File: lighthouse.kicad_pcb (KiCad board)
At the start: 2 copper layers, 78 x 58 mm, 71 parts, among them J1 GT-USB-7010ASV, J10 From_E-stop, J11 From_E-stop, J2 Conn_01x05_Pin, J3 Conn_01x10_Pin, J4 From_E-stop, J5 694106301002, J6 From_E-stop, J7 From_E-stop, J8 From_E-stop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

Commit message: Renamifications
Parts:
- J1: footprint bedroom_lights:USB_C_Receptacle_G-Switch_GT-USB-7010ASV -> lighthouse:USB_C_Receptacle_G-Switch_GT-USB-7010ASV
- SW1, SW2: footprint bedroom_lights:TS-1088R-02026_SW_SMD_3x4mm -> lighthouse:TS-1088R-02026_SW_SMD_3x4mm
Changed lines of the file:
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@@
 		(property ki_fp_filters "MountingHole*Pad*")
 		(sheetname "/")
-		(sheetfile "bedroom_lights.kicad_sch")
+		(sheetfile "lighthouse.kicad_sch")
 		(attr exclude_from_pos_files exclude_from_bom)
 		(fp_circle
@@
 		)
 	)
-	(footprint "bedroom_lights:USB_C_Receptacle_G-Switch_GT-USB-7010ASV"
+	(footprint "lighthouse:USB_C_Receptacle_G-Switch_GT-USB-7010ASV"
 		(layer "F.Cu")
 		(at 188 68 90)
@@
 		(property ki_fp_filters "MountingHole*Pad*")
 		(sheetname "/")
-		(sheetfile "bedroom_lights.kicad_sch")
+		(sheetfile "lighthouse.kicad_sch")
 		(attr exclude_from_pos_files exclude_from_bom)
 		(fp_circle
@@
 		(property ki_fp_filters "MountingHole*Pad*")
 		(sheetname "/")
-		(sheetfile "bedroom_lights.kicad_sch")
+		(sheetfile "lighthouse.kicad_sch")
 		(attr exclude_from_pos_files exclude_from_bom)
 		(fp_circle
@@
 		(property ki_fp_filters "MountingHole*Pad*")
 		(sheetname "/")
-		(sheetfile "bedroom_lights.kicad_sch")
+		(sheetfile "lighthouse.kicad_sch")
 		(attr exclude_from_pos_files exclude_from_bom)
 		(fp_circle
@@
 		)
 	)
-	(footprint "bedroom_lights:TS-1088R-02026_SW_SMD_3x4mm"
+	(footprint "lighthouse:TS-1088R-02026_SW_SMD_3x4mm"
 		(layer "F.Cu")
 		(at 173 82.5 90)
@@
 		)
 	)
-	(footprint "bedroom_lights:TS-1088R-02026_SW_SMD_3x4mm"
+	(footprint "lighthouse:TS-1088R-02026_SW_SMD_3x4mm"
 		(layer "F.Cu")
 		(at 177 82.5 -90)

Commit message: Termianl block 3d view
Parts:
- J10, J11, J4, J6, J7, J8, J9: value From_E-stop -> TB0010-500-02GR; footprint TerminalBlock:TerminalBlock_MaiXu_MX126-5.0-02P_1x02_P5.00mm -> lighthouse:TerminalBlock_TB0010-500-02GR_1x02_P5.00mm
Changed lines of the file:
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@@
 		)
 	)
-	(footprint "TerminalBlock:TerminalBlock_MaiXu_MX126-5.0-02P_1x02_P5.00mm"
+	(footprint "lighthouse:TerminalBlock_TB0010-500-02GR_1x02_P5.00mm"
 		(layer "F.Cu")
 		(at 118 74.25 -90)
@@
 		(tags "THT terminal block MaiXu MX126-5.0-02P pitch 5mm size 10.5x7.8mm drill 1.3mm pad 2.8mm")
 		(property "Reference" "J8"
-			(at 4.59 24.52 90)
+			(at 2.25 -5.12 90)
 			(layer "F.SilkS")
 			(hide yes)
@@
 			)
 		)
-		(property "Value" "From_E-stop"
+		(property "Value" "TB0010-500-02GR"
 			(at 2.25 4.92 90)
 			(layer "F.Fab")
@@
 		)
 		(embedded_fonts no)
-		(model "${KICAD9_3DMODEL_DIR}/TerminalBlock.3dshapes/TerminalBlock_MaiXu_MX126-5.0-02P_1x02_P5.00mm.wrl"
+		(model "${KIPRJMOD}/3d/TB0010-500-02GR.stp"
 			(offset
-				(xyz 0 0 0)
+				(xyz 2.5 -0.5 6.25)
 			)
 			(scale
@@
 			)
 			(rotate
-				(xyz 0 0 0)
+				(xyz -90 -0 -0)
 			)
 		)
 	)
-	(footprint "TerminalBlock:TerminalBlock_MaiXu_MX126-5.0-02P_1x02_P5.00mm"
+	(footprint "lighthouse:TerminalBlock_TB0010-500-02GR_1x02_P5.00mm"
 		(layer "F.Cu")
 		(at 118 62.75 -90)
@@
 		(tags "THT terminal block MaiXu MX126-5.0-02P pitch 5mm size 10.5x7.8mm drill 1.3mm pad 2.8mm")
 		(property "Reference" "J9"
-			(at 2.31 -43.89 90)
+			(at 2.25 -5.12 90)
 			(layer "F.SilkS")
 			(hide yes)
@@
 			)
 		)
-		(property "Value" "From_E-stop"
+		(property "Value" "TB0010-500-02GR"
 			(at 2.25 4.92 90)
 			(layer "F.Fab")
@@
 		)
 		(embedded_fonts no)
-		(model "${KICAD9_3DMODEL_DIR}/TerminalBlock.3dshapes/TerminalBlock_MaiXu_MX126-5.0-02P_1x02_P5.00mm.wrl"
+		(model "${KIPRJMOD}/3d/TB0010-500-02GR.stp"
 			(offset
-				(xyz 0 0 0)
+				(xyz 2.5 -0.5 6.25)
 			)
 			(scale
@@
 			)
 			(rotate
-				(xyz 0 0 0)
+				(xyz -90 -0 -0)
 			)
 		)
@@
 		(embedded_fonts no)
 	)
-	(footprint "TerminalBlock:TerminalBlock_MaiXu_MX126-5.0-02P_1x02_P5.00mm"
+	(footprint "lighthouse:TerminalBlock_TB0010-500-02GR_1x02_P5.00mm"
 		(layer "F.Cu")
 		(at 186.9675 90.25 90)
@@
 		(tags "THT terminal block MaiXu MX126-5.0-02P pitch 5mm size 10.5x7.8mm drill 1.3mm pad 2.8mm")
 		(property "Reference" "J6"
-			(at 2.25 -5.12 90)
+			(at 2.25 -5.12 270)
 			(layer "F.SilkS")
 			(hide yes)
@@
 			)
 		)
-		(property "Value" "From_E-stop"
-			(at 2.25 4.92 90)
+		(property "Value" "TB0010-500-02GR"
+			(at 2.25 4.92 270)
 			(layer "F.Fab")
 			(effects
@@
 		)
 		(property "Datasheet" "~"
-			(at 0 0 90)
+			(at 0 0 270)
 			(layer "F.Fab")
 			(hide yes)
@@
 		)
 		(property "Description" "Generic screw terminal, single row, 01x02, script generated (kicad-library-utils/schlib/autogen/connector/)"
-			(at 0 0 90)
+			(at 0 0 270)
 			(layer "F.Fab")
 			(hide yes)
@@
 		)
 		(fp_text user "${REFERENCE}"
-			(at 2.25 2.65 90)
+			(at 2.25 2.65 270)
 			(layer "F.Fab")
 			(effects
@@
 		)
 		(embedded_fonts no)
-		(model "${KICAD9_3DMODEL_DIR}/TerminalBlock.3dshapes/TerminalBlock_MaiXu_MX126-5.0-02P_1x02_P5.00mm.wrl"
+		(model "${KIPRJMOD}/3d/TB0010-500-02GR.stp"
 			(offset
-				(xyz 0 0 0)
+				(xyz 2.5 -0.5 6.25)
 			)
 			(scale
@@
 			)
 			(rotate
-				(xyz 0 0 0)
+				(xyz -90 -0 -0)
 			)
 		)
@@
 		)
 	)
-	(footprint "TerminalBlock:TerminalBlock_MaiXu_MX126-5.0-02P_1x02_P5.00mm"
+	(footprint "lighthouse:TerminalBlock_TB0010-500-02GR_1x02_P5.00mm"
 		(layer "F.Cu")
 		(at 118 97.25 -90)
@@
 			)
 		)
-		(property "Value" "From_E-stop"
+		(property "Value" "TB0010-500-02GR"
 			(at 2.25 4.92 90)
 			(layer "F.Fab")
@@
 		)
 		(embedded_fonts no)
-		(model "${KICAD9_3DMODEL_DIR}/TerminalBlock.3dshapes/TerminalBlock_MaiXu_MX126-5.0-02P_1x02_P5.00mm.wrl"
+		(model "${KIPRJMOD}/3d/TB0010-500-02GR.stp"
 			(offset
-				(xyz 0 0 0)
+				(xyz 2.5 -0.5 6.25)
 			)
 			(scale
@@
 			)
 			(rotate
-				(xyz 0 0 0)
+				(xyz -90 -0 -0)
 			)
 		)
 	)
-	(footprint "TerminalBlock:TerminalBlock_MaiXu_MX126-5.0-02P_1x02_P5.00mm"
+	(footprint "lighthouse:TerminalBlock_TB0010-500-02GR_1x02_P5.00mm"
 		(layer "F.Cu")
 		(at 132.75 106.9675)
@@
 		(tags "THT terminal block MaiXu MX126-5.0-02P pitch 5mm size 10.5x7.8mm drill 1.3mm pad 2.8mm")
 		(property "Reference" "J4"
-			(at 2.25 -5.12 0)
+			(at 2.25 -5.12 180)
 			(layer "F.SilkS")
 			(hide yes)
@@
 			)
 		)
-		(property "Value" "From_E-stop"
-			(at 2.25 4.92 0)
+		(property "Value" "TB0010-500-02GR"
+			(at 2.25 4.92 180)
 			(layer "F.Fab")
 			(effects
@@
 		)
 		(property "Datasheet" "~"
-			(at 0 0 0)
+			(at 0 0 180)
 			(layer "F.Fab")
 			(hide yes)
@@
 		)
 		(property "Description" "Generic screw terminal, single row, 01x02, script generated (kicad-library-utils/schlib/autogen/connector/)"
-			(at 0 0 0)
+			(at 0 0 180)
 			(layer "F.Fab")
 			(hide yes)
@@
 		)
 		(fp_text user "${REFERENCE}"
-			(at 2.25 2.65 0)
+			(at 2.25 2.65 180)
 			(layer "F.Fab")
 			(effects
@@
 		)
 		(embedded_fonts no)
-		(model "${KICAD9_3DMODEL_DIR}/TerminalBlock.3dshapes/TerminalBlock_MaiXu_MX126-5.0-02P_1x02_P5.00mm.wrl"
+		(model "${KIPRJMOD}/3d/TB0010-500-02GR.stp"
 			(offset
-				(xyz 0 0 0)
+				(xyz 2.5 -0.5 6.25)
 			)
 			(scale
@@
 			)
 			(rotate
-				(xyz 0 0 0)
+				(xyz -90 -0 -0)
 			)
 		)
@@
 		)
 	)
-	(footprint "TerminalBlock:TerminalBlock_MaiXu_MX126-5.0-02P_1x02_P5.00mm"
+	(footprint "lighthouse:TerminalBlock_TB0010-500-02GR_1x02_P5.00mm"
 		(layer "F.Cu")
 		(at 118 85.75 -90)
@@
 			)
 		)
-		(property "Value" "From_E-stop"
+		(property "Value" "TB0010-500-02GR"
 			(at 2.25 4.92 90)
 			(layer "F.Fab")
@@
 		)
 		(embedded_fonts no)
-		(model "${KICAD9_3DMODEL_DIR}/TerminalBlock.3dshapes/TerminalBlock_MaiXu_MX126-5.0-02P_1x02_P5.00mm.wrl"
+		(model "${KIPRJMOD}/3d/TB0010-500-02GR.stp"
 			(offset
-				(xyz 0 0 0)
+				(xyz 2.5 -0.5 6.25)
 			)
 			(scale
@@
 			)
 			(rotate
-				(xyz 0 0 0)
+				(xyz -90 -0 -0)
 			)
 		)
@@
 		)
 	)
-	(footprint "TerminalBlock:TerminalBlock_MaiXu_MX126-5.0-02P_1x02_P5.00mm"
+	(footprint "lighthouse:TerminalBlock_TB0010-500-02GR_1x02_P5.00mm"
 		(layer "F.Cu")
 		(at 144.75 106.9675)
@@
 		(tags "THT terminal block MaiXu MX126-5.0-02P pitch 5mm size 10.5x7.8mm drill 1.3mm pad 2.8mm")
 		(property "Reference" "J7"
-			(at 2.25 -5.12 0)
+			(at 2.25 -5.12 180)
 			(layer "F.SilkS")
 			(hide yes)
@@
 			)
 		)
-		(property "Value" "From_E-stop"
-			(at 2.25 4.92 0)
+		(property "Value" "TB0010-500-02GR"
+			(at 2.25 4.92 180)
 			(layer "F.Fab")
 			(effects
@@
 		)
 		(property "Datasheet" "~"
-			(at 0 0 0)
+			(at 0 0 180)
 			(layer "F.Fab")
 			(hide yes)
@@
 		)
 		(property "Description" "Generic screw terminal, single row, 01x02, script generated (kicad-library-utils/schlib/autogen/connector/)"
-			(at 0 0 0)
+			(at 0 0 180)
 			(layer "F.Fab")
 			(hide yes)
@@
 		)
 		(fp_text user "${REFERENCE}"
-			(at 2.25 2.65 0)
+			(at 2.25 2.65 180)
 			(layer "F.Fab")
 			(effects
@@
 		)
 		(embedded_fonts no)
-		(model "${KICAD9_3DMODEL_DIR}/TerminalBlock.3dshapes/TerminalBlock_MaiXu_MX126-5.0-02P_1x02_P5.00mm.wrl"
+		(model "${KIPRJMOD}/3d/TB0010-500-02GR.stp"
 			(offset
-				(xyz 0 0 0)
+				(xyz 2.5 -0.5 6.25)
 			)
 			(scale
@@
 			)
 			(rotate
-				(xyz 0 0 0)
+				(xyz -90 -0 -0)
 			)
 		)

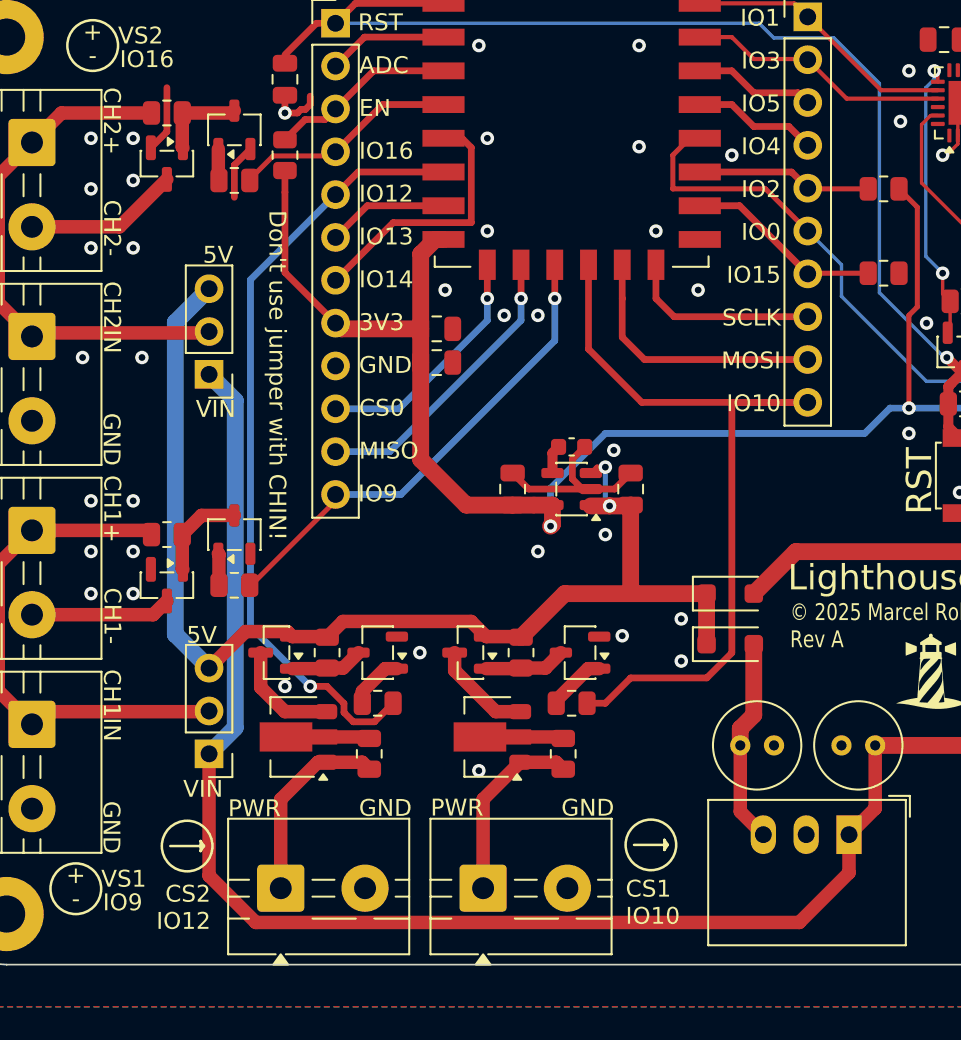
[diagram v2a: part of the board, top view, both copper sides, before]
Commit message: Correct unusable FLASH SPI pins
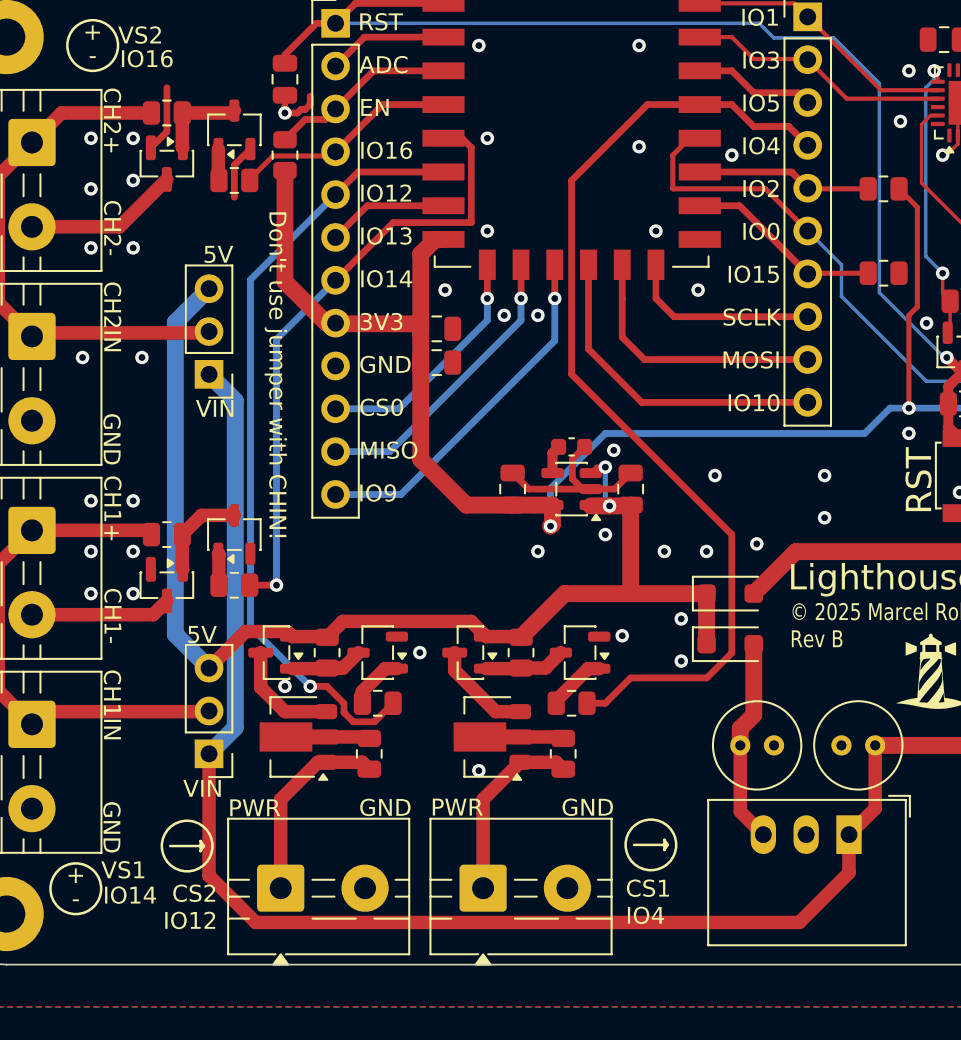
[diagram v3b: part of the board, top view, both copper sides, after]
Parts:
- Q3, Q5, Q7, Q9: value S8050 -> MMSS8050-H-TP
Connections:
- J2 pad 12: /MCU/LSS1 -> /MCU/GPIO9
- J2 pad 7: /MCU/GPIO14 -> /MCU/LSS1
- J3 pad 10: /MCU/CSO1 -> /MCU/GPIO10
- J3 pad 4: /MCU/GPIO4 -> /MCU/CSO1
- U2 pad 11: /MCU/LSS1 -> /MCU/GPIO9
- U2 pad 12: /MCU/CSO1 -> /MCU/GPIO10
- U2 pad 19: /MCU/GPIO4 -> /MCU/CSO1
- U2 pad 5: /MCU/GPIO14 -> /MCU/LSS1
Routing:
- net /MCU/GPIO9: track 0.00 -> 21.7 mm, vias 0 -> 1
- net /MCU/GPIO10: track 0.00 -> 19.3 mm
- net /MCU/GPIO14: track 15.8 -> 0.00 mm
- net /MCU/CSO1: track 48.5 -> 58.6 mm
- net /MCU/LSS1: track 28.8 -> 37.0 mm
- net /MCU/GPIO4: track 7.40 -> 0.00 mm
- net GND: vias 53 -> 59
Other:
- board text added: "CS1 IO4"
- board text added: "© 2025 Marcel Robitaille Rev B"
- board text removed: "CS1 IO10"
- board text removed: "© 2025 Marcel Robitaille Rev A"
